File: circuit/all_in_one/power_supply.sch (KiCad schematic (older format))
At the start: 22 parts, among them Q1 2SB647, Q2 2SK2611, U1 SMD_7805, U2 MC34063A

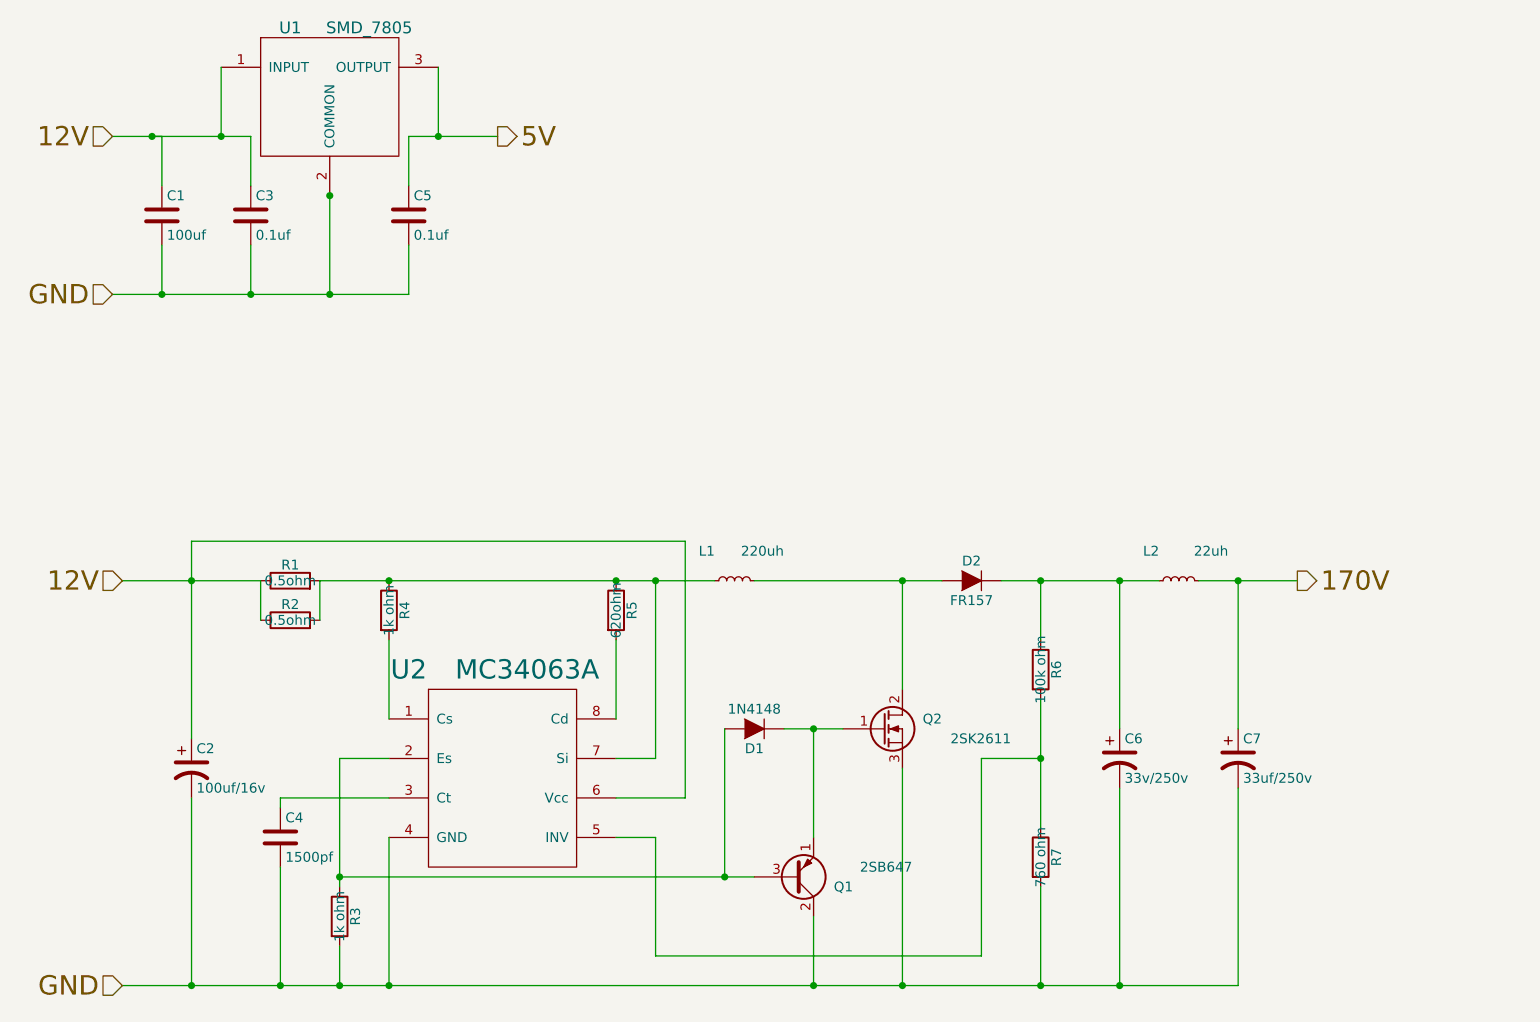
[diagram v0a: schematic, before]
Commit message: New hardware is almost finished
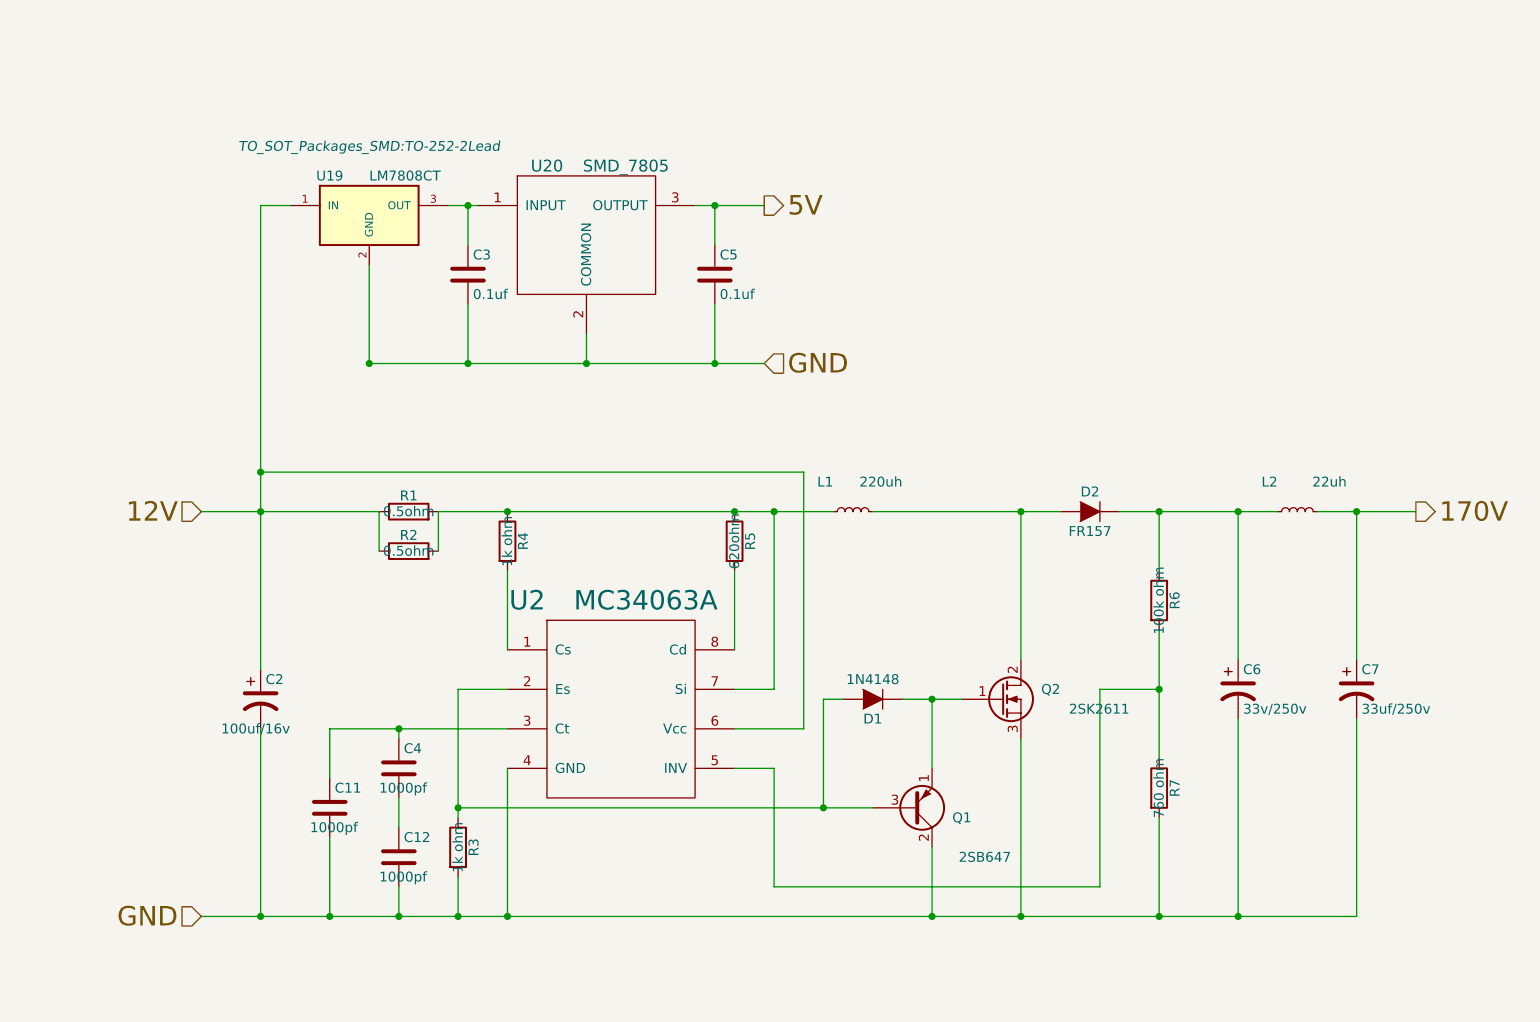
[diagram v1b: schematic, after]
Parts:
- removed C1: 100uf, Capacitors_Tantalum_SMD:TantalC_SizeC_EIA-6032_HandSoldering, symbol C
- removed U1: SMD_7805, TO_SOT_Packages_SMD:TO-252-2Lead, symbol SMD_7805
- added C11, C12: 1000pf, Capacitors_SMD:C_0805_HandSoldering, symbol C
- added U19: LM7808CT, TO_SOT_Packages_SMD:TO-252-2Lead, symbol LM7808CT
- added U20: SMD_7805, TO_SOT_Packages_SMD:TO-252-2Lead, symbol SMD_7805
- C2: footprint Capacitors_Tantalum_SMD:TantalC_SizeC_EIA-6032_HandSoldering -> Capacitors_SMD:c_elec_6.3x5.3
- C4: value 1500pf -> 1000pf
- R1, R2, R3, R4, R5, R6, R7: footprint Resistors_SMD:R_0805_HandSoldering -> Resistors_SMD:R_1206_HandSoldering
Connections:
- net 12V: now also U19.1 (IN); no longer C3.1
- net 5V: now also U20.3 (OUTPUT)
- net GND: now also C11.2, C12.2, U19.2 (GND), U20.2 (COMMON); no longer C4.2
- net at C4.1, U2.3 (Ct): now also C11.1
- new net: C12.1, C4.2
- new net: C3.1, U19.3 (OUT), U20.1 (INPUT)
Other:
- moved on the sheet: C2, C4, C6, C7, D1, D2, L1, L2, Q1, Q2, R1, R2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
